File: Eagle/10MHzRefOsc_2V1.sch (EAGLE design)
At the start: 82 parts, among them CON1 TYCO-AMP_USBUSB-B_SMT, CON2 HEADER-2X5SMD, CON3 SD-73100-0105, CON4 AVR-ISP-6SMD, CON5 AVR-JTAG-10SMD, CON6 HEADER-2X3SMD, CON7 MCX-J-P-X-RA-SM1, IC1 ATmega328-P, IC2 LC4032V_XXT44, IC3 74HCT221D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

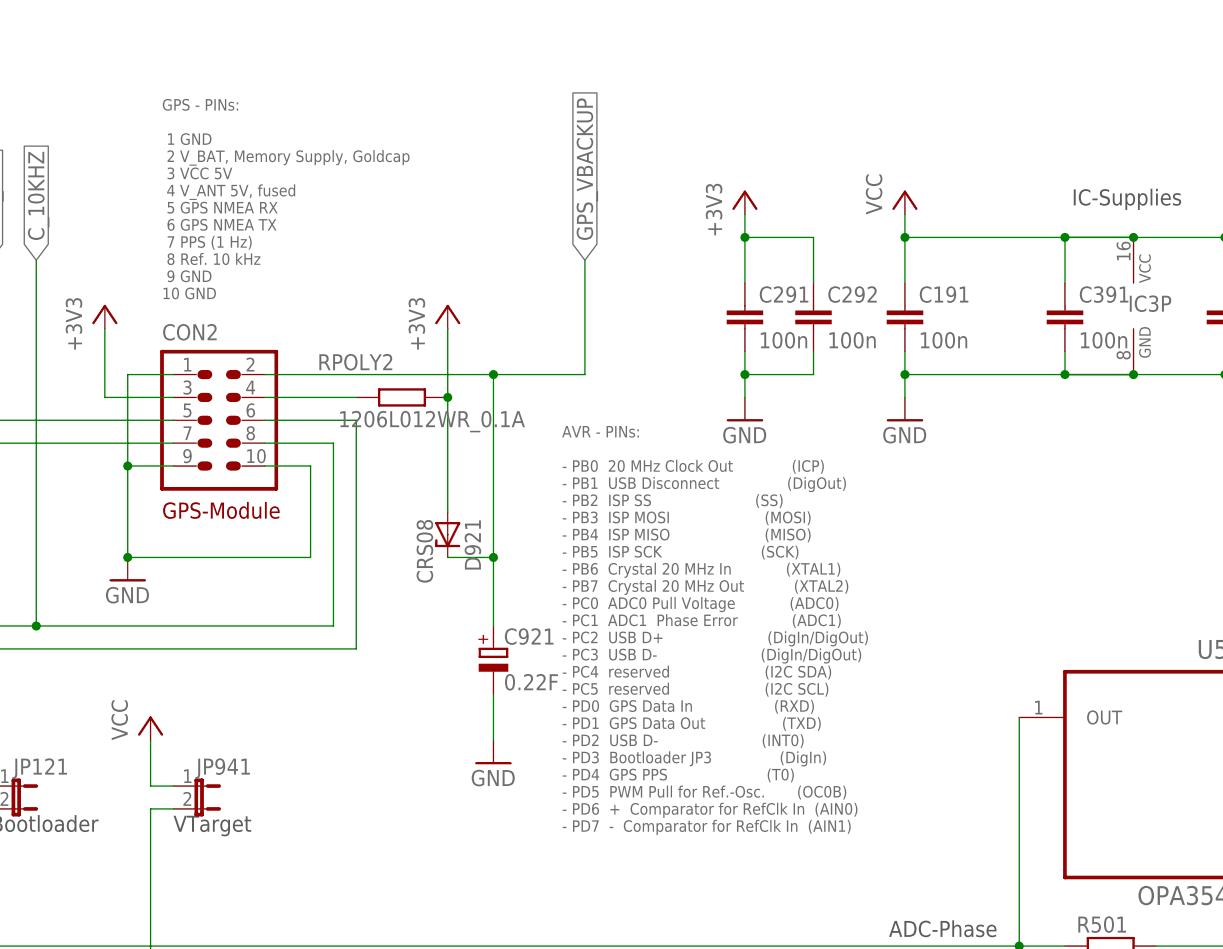
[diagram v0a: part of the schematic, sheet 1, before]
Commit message: HW_V2.1.1 - GPS connector - fixed 5V to 3V3 in info block
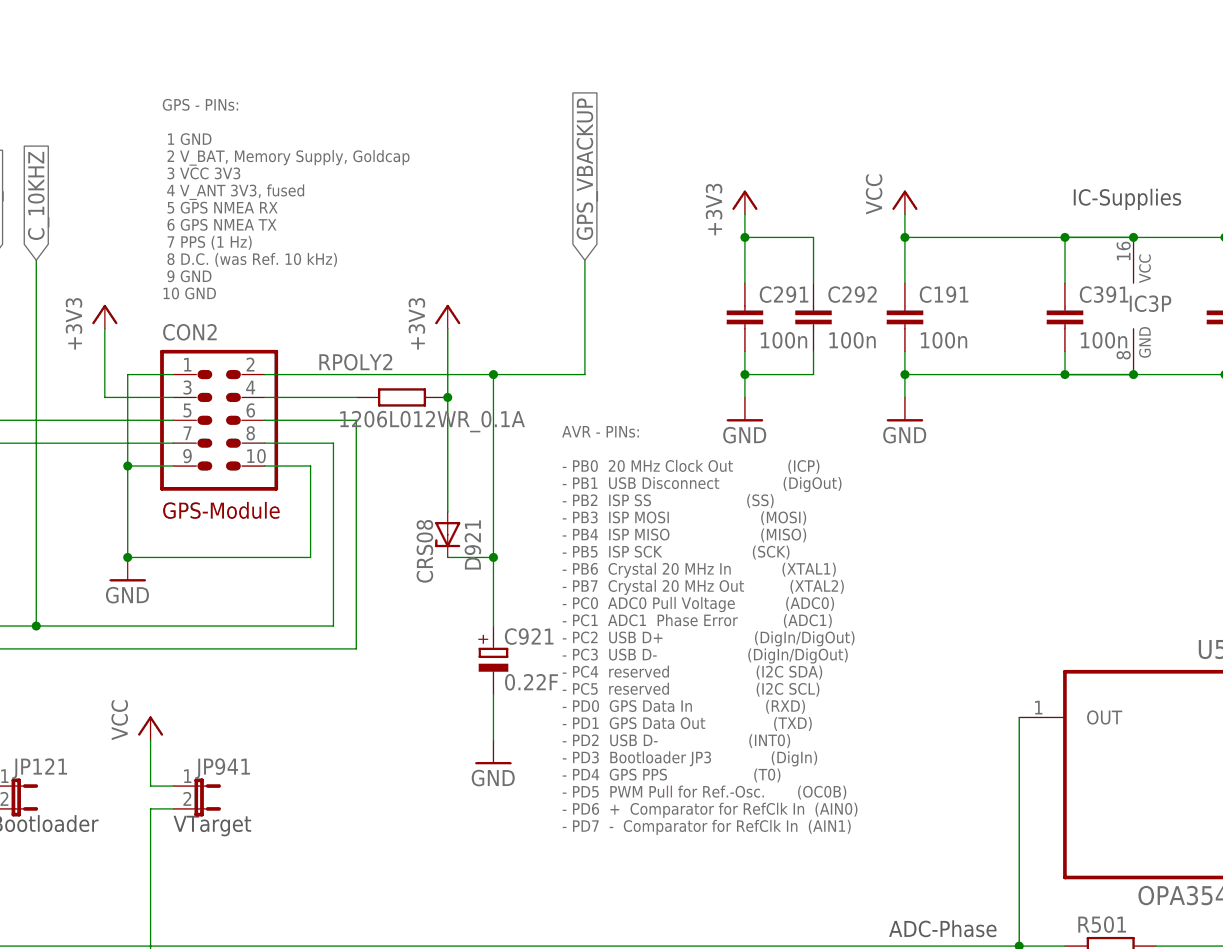
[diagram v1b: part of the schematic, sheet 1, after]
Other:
- note added: "GPS - PINs: 1 GND 2 V_BAT, Memory Supply, Goldcap 3 VCC 3V3 4 V_ANT 3V3, fused 5 GPS NMEA RX 6 GPS NMEA TX 7 PPS (1 Hz) 8 D.C. (was Ref. 10 kHz) 9 GND 10 GND"
- note removed: "GPS - PINs: 1 GND 2 V_BAT, Memory Supply, Goldcap 3 VCC 5V 4 V_ANT 5V, fused 5 GPS NMEA RX 6 GPS NMEA TX 7 PPS (1 Hz) 8 Ref. 10 kHz 9 GND 10 GND"
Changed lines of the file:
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@@
 <?xml version="1.0" encoding="utf-8"?>
 <!DOCTYPE eagle SYSTEM "eagle.dtd">
-<eagle version="7.2.0">
+<eagle version="7.7.0">
 <drawing>
 <settings>
@@
 <text x="10.414" y="115.062" size="1.778" layer="94">USB-B</text>
 <text x="243.84" y="203.2" size="1.27" layer="96" font="fixed">AVR - PINs:
-- PB0  20 MHz Clock Out             (ICP)
-- PB1  USB Disconnect               (DigOut)
-- PB2  ISP SS                       (SS)
-- PB3  ISP MOSI                     (MOSI)
-- PB4  ISP MISO                     (MISO)
-- PB5  ISP SCK                      (SCK)
-- PB6  Crystal 20 MHz In            (XTAL1)
-- PB7  Crystal 20 MHz Out           (XTAL2)
-- PC0  ADC0 Pull Voltage            (ADC0)
-- PC1  ADC1  Phase Error            (ADC1)
-- PC2  USB D+                       (DigIn/DigOut)
-- PC3  USB D-                       (DigIn/DigOut)
-- PC4  reserved                     (I2C SDA)
-- PC5  reserved                     (I2C SCL)
-- PD0  GPS Data In                  (RXD)
-- PD1  GPS Data Out                 (TXD)
-- PD2  USB D-                       (INT0)
-- PD3  Bootloader JP3               (DigIn)
-- PD4  GPS PPS                      (T0)
+- PB0  20 MHz Clock Out            (ICP)
+- PB1  USB Disconnect              (DigOut)
+- PB2  ISP SS                     (SS)
+- PB3  ISP MOSI                    (MOSI)
+- PB4  ISP MISO                    (MISO)
+- PB5  ISP SCK                    (SCK)
+- PB6  Crystal 20 MHz In           (XTAL1)
+- PB7  Crystal 20 MHz Out          (XTAL2)
+- PC0  ADC0 Pull Voltage           (ADC0)
+- PC1  ADC1  Phase Error          (ADC1)
+- PC2  USB D+                    (DigIn/DigOut)
+- PC3  USB D-                    (DigIn/DigOut)
+- PC4  reserved                   (I2C SDA)
+- PC5  reserved                   (I2C SCL)
+- PD0  GPS Data In                (RXD)
+- PD1  GPS Data Out               (TXD)
+- PD2  USB D-                    (INT0)
+- PD3  Bootloader JP3             (DigIn)
+- PD4  GPS PPS                   (T0)
 - PD5  PWM Pull for Ref.-Osc.       (OC0B)
 - PD6  +  Comparator for RefClk In  (AIN0)
@@
  1 GND
  2 V_BAT, Memory Supply, Goldcap
- 3 VCC 5V
- 4 V_ANT 5V, fused
+ 3 VCC 3V3
+ 4 V_ANT 3V3, fused
  5 GPS NMEA RX
  6 GPS NMEA TX
  7 PPS (1 Hz)
- 8 Ref. 10 kHz
+ 8 D.C. (was Ref. 10 kHz)
  9 GND
 10 GND</text>
@@
 <wire x1="121.92" y1="251.46" x2="121.92" y2="248.92" width="0.1524" layer="91"/>
 <pinref part="CON3" gate="G$1" pin="3"/>
-<pinref part="CON3" gate="G$1" pin="3"/>
 <junction x="121.92" y="251.46"/>
